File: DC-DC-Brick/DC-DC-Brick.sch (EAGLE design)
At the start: 21 parts

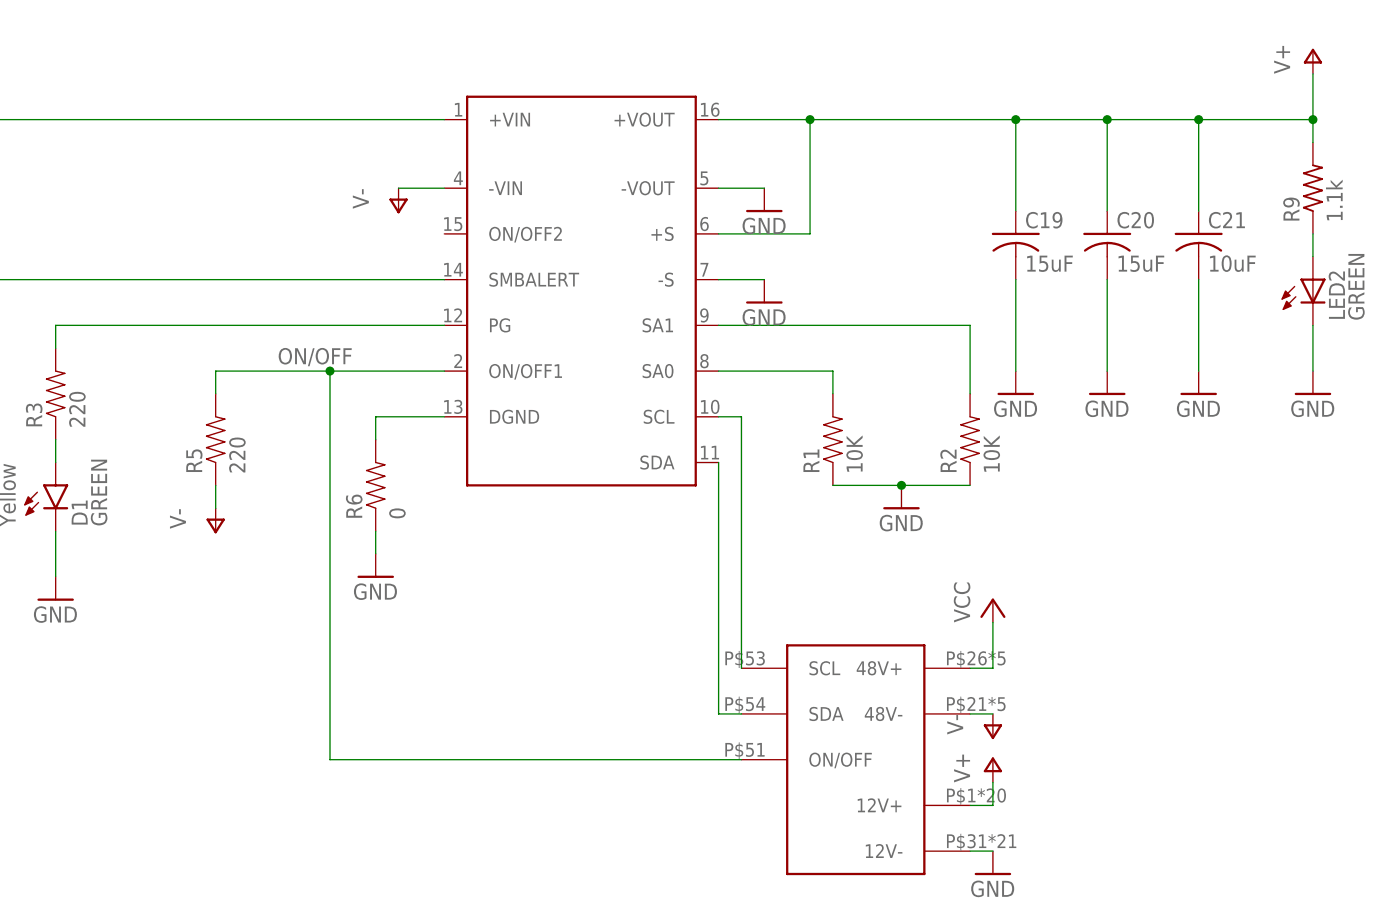
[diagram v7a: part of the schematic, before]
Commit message: cleaned up poligons
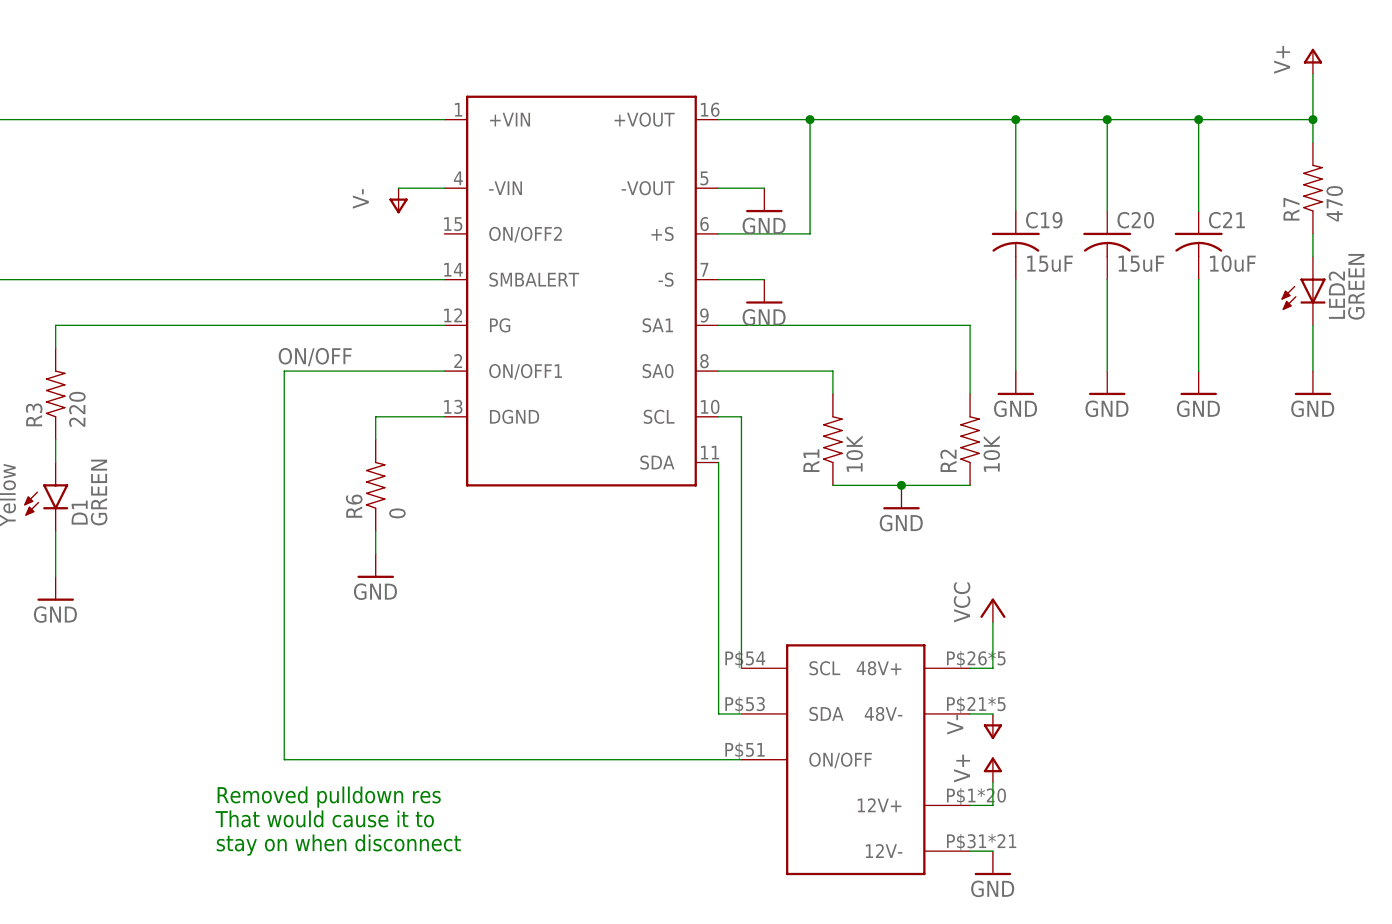
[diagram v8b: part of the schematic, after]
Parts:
- removed R5: 220, SparkFun-Resistors:1KOHM-1/10W-1%(0603)
- removed R9: 1.1k, resistor:R-US_R1206
- added R7: 470, SparkFun-Resistors:470OHM1/10W1%(0603)
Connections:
- net N$12: now also R7.1; no longer R9.1
- net ON/OFF: no longer R5.2
- net V+: now also R7.2; no longer R9.2
- net V-: no longer R5.1
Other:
- note added: "Removed pulldown res That would cause it to stay on when disconnect"
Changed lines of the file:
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@@
 <?xml version="1.0" encoding="utf-8"?>
 <!DOCTYPE eagle SYSTEM "eagle.dtd">
-<eagle version="7.6.0">
+<eagle version="7.7.0">
 <drawing>
 <settings>
@@
 <layers>
 <layer number="1" name="Top" color="4" fill="1" visible="no" active="no"/>
+<layer number="2" name="Route2" color="1" fill="3" visible="no" active="no"/>
+<layer number="3" name="Route3" color="4" fill="3" visible="no" active="no"/>
+<layer number="14" name="Route14" color="1" fill="6" visible="no" active="no"/>
+<layer number="15" name="Route15" color="4" fill="6" visible="no" active="no"/>
 <layer number="16" name="Bottom" color="1" fill="1" visible="no" active="no"/>
 <layer number="17" name="Pads" color="2" fill="1" visible="no" active="no"/>
@@
 </part>
 <part name="GND19" library="supply1" deviceset="GND" device=""/>
-<part name="R9" library="resistor" deviceset="R-US_" device="R1206" value="1.1k">
-<attribute name="BOM" value="INCLUDE"/>
-<attribute name="PARTNO" value="RNCP1206FTD1K10CT-ND"/>
-</part>
 <part name="GND40" library="supply1" deviceset="GND" device=""/>
 <part name="C19" library="rcl" deviceset="C-US" device="C3216" value="15uF"/>
@@
 <part name="GND8" library="supply1" deviceset="GND" device=""/>
 <part name="P-3" library="supply1" deviceset="V-" device=""/>
-<part name="R5" library="SparkFun-Resistors" deviceset="1KOHM-1/10W-1%(0603)" device="" value="220"/>
-<part name="P-4" library="supply1" deviceset="V-" device=""/>
+<part name="R7" library="SparkFun-Resistors" deviceset="470OHM1/10W1%(0603)" device="" value="470"/>
 </parts>
 <sheets>
 <sheet>
 <plain>
+<text x="205.74" y="81.28" size="1.778" layer="91">Removed pulldown res
+That would cause it to
+stay on when disconnect</text>
 </plain>
 <instances>
@@
 </instance>
 <instance part="GND19" gate="1" x="327.66" y="132.08"/>
-<instance part="R9" gate="G$1" x="327.66" y="154.94" rot="R90">
-<attribute name="PARTNO" value="RNCP1206FTD1K10CT-ND" x="327.66" y="154.94" size="0.0254" layer="96" font="vector" display="off"/>
-<attribute name="BOM" value="INCLUDE" x="327.66" y="154.94" size="0.0254" layer="96" font="vector" display="off"/>
-</instance>
 <instance part="GND40" gate="1" x="314.96" y="132.08"/>
 <instance part="C19" gate="G$1" x="294.64" y="149.86"/>
@@
 <instance part="GND8" gate="1" x="292.1" y="78.74"/>
 <instance part="P-3" gate="1" x="292.1" y="93.98"/>
-<instance part="R5" gate="G$1" x="205.74" y="127" rot="R90"/>
-<instance part="P-4" gate="1" x="205.74" y="116.84"/>
+<instance part="R7" gate="G$1" x="327.66" y="154.94" rot="R90"/>
 </instances>
 <busses>
@@
 <wire x1="289.56" y1="96.52" x2="292.1" y2="96.52" width="0.1524" layer="91"/>
 </segment>
-<segment>
-<pinref part="R5" gate="G$1" pin="1"/>
-<pinref part="P-4" gate="1" pin="V-"/>
-<wire x1="205.74" y1="121.92" x2="205.74" y2="119.38" width="0.1524" layer="91"/>
-</segment>
 </net>
 <net name="N$12" class="0">
 <segment>
-<pinref part="R9" gate="G$1" pin="1"/>
 <pinref part="LED2" gate="G$1" pin="A"/>
 <wire x1="327.66" y1="149.86" x2="327.66" y2="147.32" width="0.1524" layer="91"/>
+<pinref part="R7" gate="G$1" pin="1"/>
 </segment>
 </net>
@@
 </segment>
 <segment>
-<pinref part="R9" gate="G$1" pin="2"/>
 <wire x1="327.66" y1="162.56" x2="327.66" y2="160.02" width="0.1524" layer="91"/>
 <junction x="327.66" y="162.56"/>
@@
 <junction x="271.78" y="162.56"/>
 <junction x="294.64" y="162.56"/>
+<pinref part="R7" gate="G$1" pin="2"/>
 </segment>
 </net>
@@
 <segment>
 <pinref part="U$1" gate="G$1" pin="ON/OFF1"/>
-<wire x1="231.14" y1="134.62" x2="218.44" y2="134.62" width="0.1524" layer="91"/>
-<wire x1="218.44" y1="134.62" x2="218.44" y2="91.44" width="0.1524" layer="91"/>
+<wire x1="231.14" y1="134.62" x2="213.36" y2="134.62" width="0.1524" layer="91"/>
+<wire x1="213.36" y1="134.62" x2="213.36" y2="91.44" width="0.1524" layer="91"/>
 <pinref part="U$3" gate="G$1" pin="ON/OFF"/>
-<wire x1="218.44" y1="91.44" x2="264.16" y2="91.44" width="0.1524" layer="91"/>
-<pinref part="R5" gate="G$1" pin="2"/>
-<wire x1="218.44" y1="134.62" x2="205.74" y2="134.62" width="0.1524" layer="91"/>
-<wire x1="205.74" y1="134.62" x2="205.74" y2="132.08" width="0.1524" layer="91"/>
-<junction x="218.44" y="134.62"/>
+<wire x1="213.36" y1="91.44" x2="264.16" y2="91.44" width="0.1524" layer="91"/>
 <label x="220.98" y="137.16" size="1.778" layer="95" rot="R180"/>
 </segment>
@@
 </schematic>
 </drawing>
+<compatibility>
+<note version="6.3" minversion="6.2.2" severity="warning">
+Since Version 6.2.2 text objects can contain more than one line,
+which will not be processed correctly with this version.
+</note>
+</compatibility>
 </eagle>
